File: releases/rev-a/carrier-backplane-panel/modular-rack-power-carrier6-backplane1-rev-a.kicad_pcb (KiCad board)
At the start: 4 copper layers, 163.8 x 237.3 mm, 729 parts

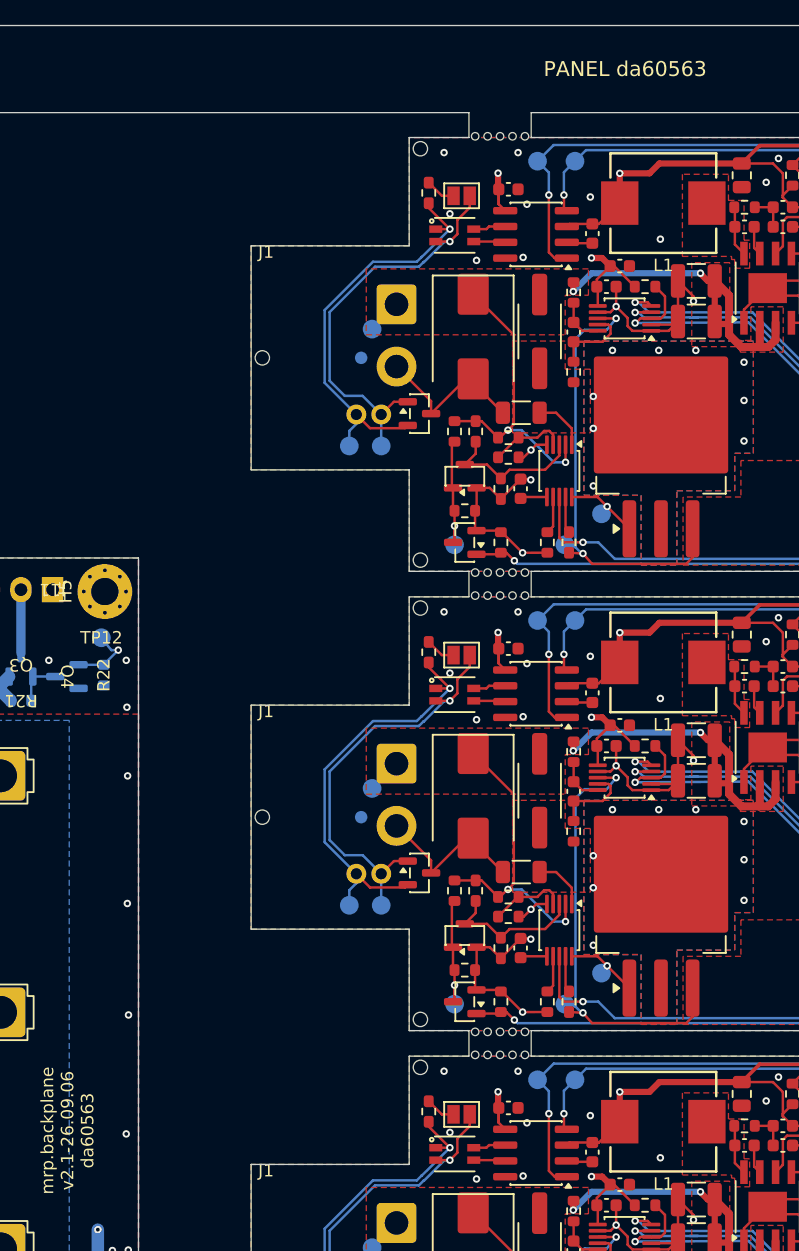
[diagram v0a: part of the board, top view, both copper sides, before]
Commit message: Regenerate production outputs without DC terminal
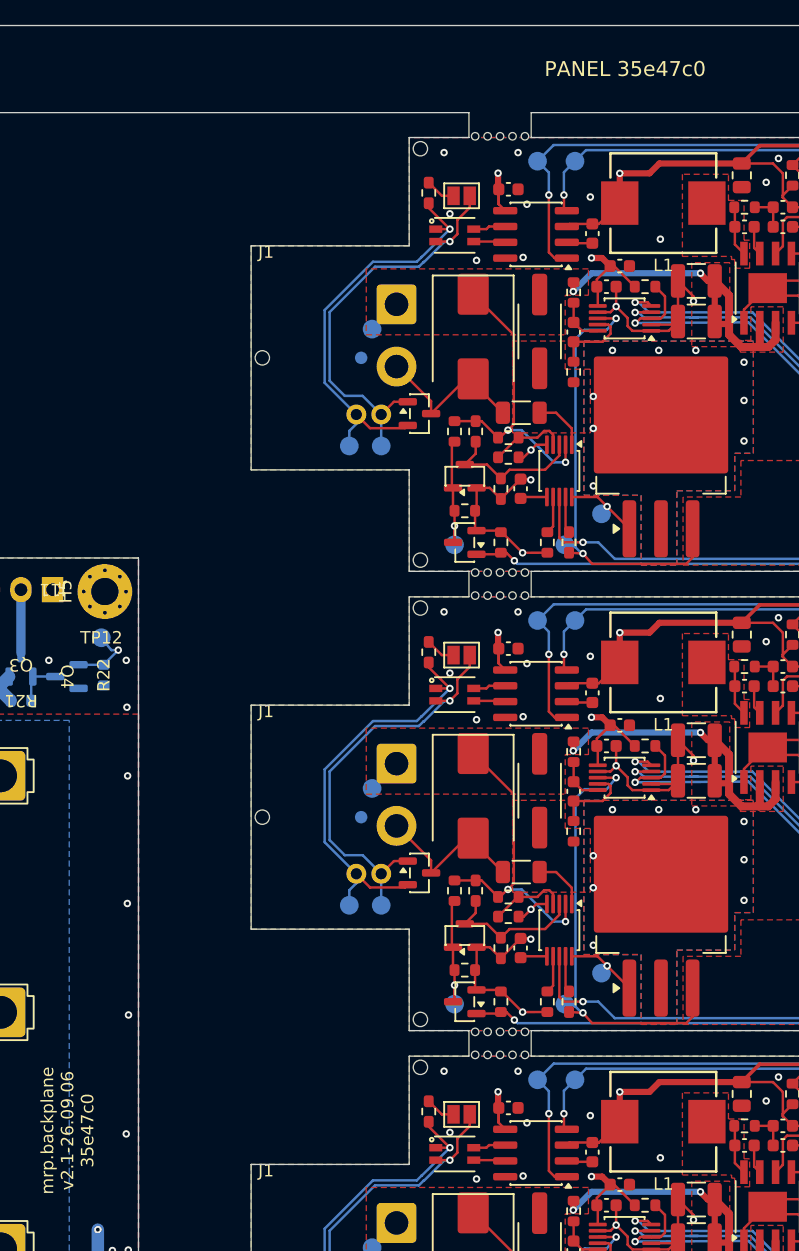
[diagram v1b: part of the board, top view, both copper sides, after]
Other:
- board text added: "PANEL 35e47c0"
- board text added: "mrp.backplane v2.1-26.09.06 35e47c0"
- board text added: "mrp.carrier v2.1-26.09.06 35e47c0"
- board text removed: "PANEL da60563"
- board text removed: "mrp.backplane v2.1-26.09.06 da60563"
- board text removed: "mrp.carrier v2.1-26.09.06 da60563"
